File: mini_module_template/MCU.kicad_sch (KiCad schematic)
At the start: 35 parts, among them J3 SWD, SW1 USR_BTN, SW2 BOOT0, SW3 NRST, U1 STM32F303CBTx, U2 FM24CL16B, Y1 8MHz

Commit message: Leyout rev 1
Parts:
- removed J3: SWD, Connector_PinHeader_2.54mm:PinHeader_1x04_P2.54mm_Vertical, symbol Connector_Generic:Conn_01x04
- removed R10, R13, R17: 10k, Resistor_SMD:R_0402_1005Metric, symbol Device:R
- added J1: SWD, Connector_PinSocket_2.54mm:PinSocket_1x05_P2.54mm_Vertical, symbol Connector_Generic:Conn_01x05
- C11: renamed from C3; value 16p -> 17p
- C12: renamed from C4; value 16p -> 17p
- R1: renamed from R15; now not fitted
- R8: renamed from R3; now not fitted
- SW1: renamed from SW2; footprint Button_Switch_SMD:SW_SPST_PTS810 -> Button_Switch_THT:SW_Tactile_SPST_Angled_PTS645Vx58-2LFS; now not fitted
- SW2: renamed from SW3; footprint Button_Switch_SMD:SW_SPST_PTS810 -> Button_Switch_THT:SW_Tactile_SPST_Angled_PTS645Vx58-2LFS
- SW3: renamed from SW1; footprint Button_Switch_SMD:SW_SPST_PTS810 -> Button_Switch_THT:SW_Tactile_SPST_Angled_PTS645Vx58-2LFS; now not fitted
- renumbered C5 to C1, C1 to C10, C6 to C2, C7 to C3, C8 to C4, C9 to C5, C10 to C6, C11 to C7, C12 to C8, C2 to C9, D1 to D2, D2 to D3, R2 to R10, R19 to R2, R12 to R3, R16 to R4, R11 to R5, R14 to R6, R18 to R7, R1 to R9
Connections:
- net +3V3: now also J1.1 (Pin_1)
- net GND: now also J1.5 (Pin_5)
- net NRST: now also J1.2 (Pin_2)
- net SWCLK: now also J1.4 (Pin_4)
- net SWDIO: now also J1.3 (Pin_3)
- net PA15: no longer names the net of U1.38 (PA15)
- no-connect marks 0 -> 4
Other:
- note removed: "optional pulldown resistors"
- moved on the sheet: R7, U2

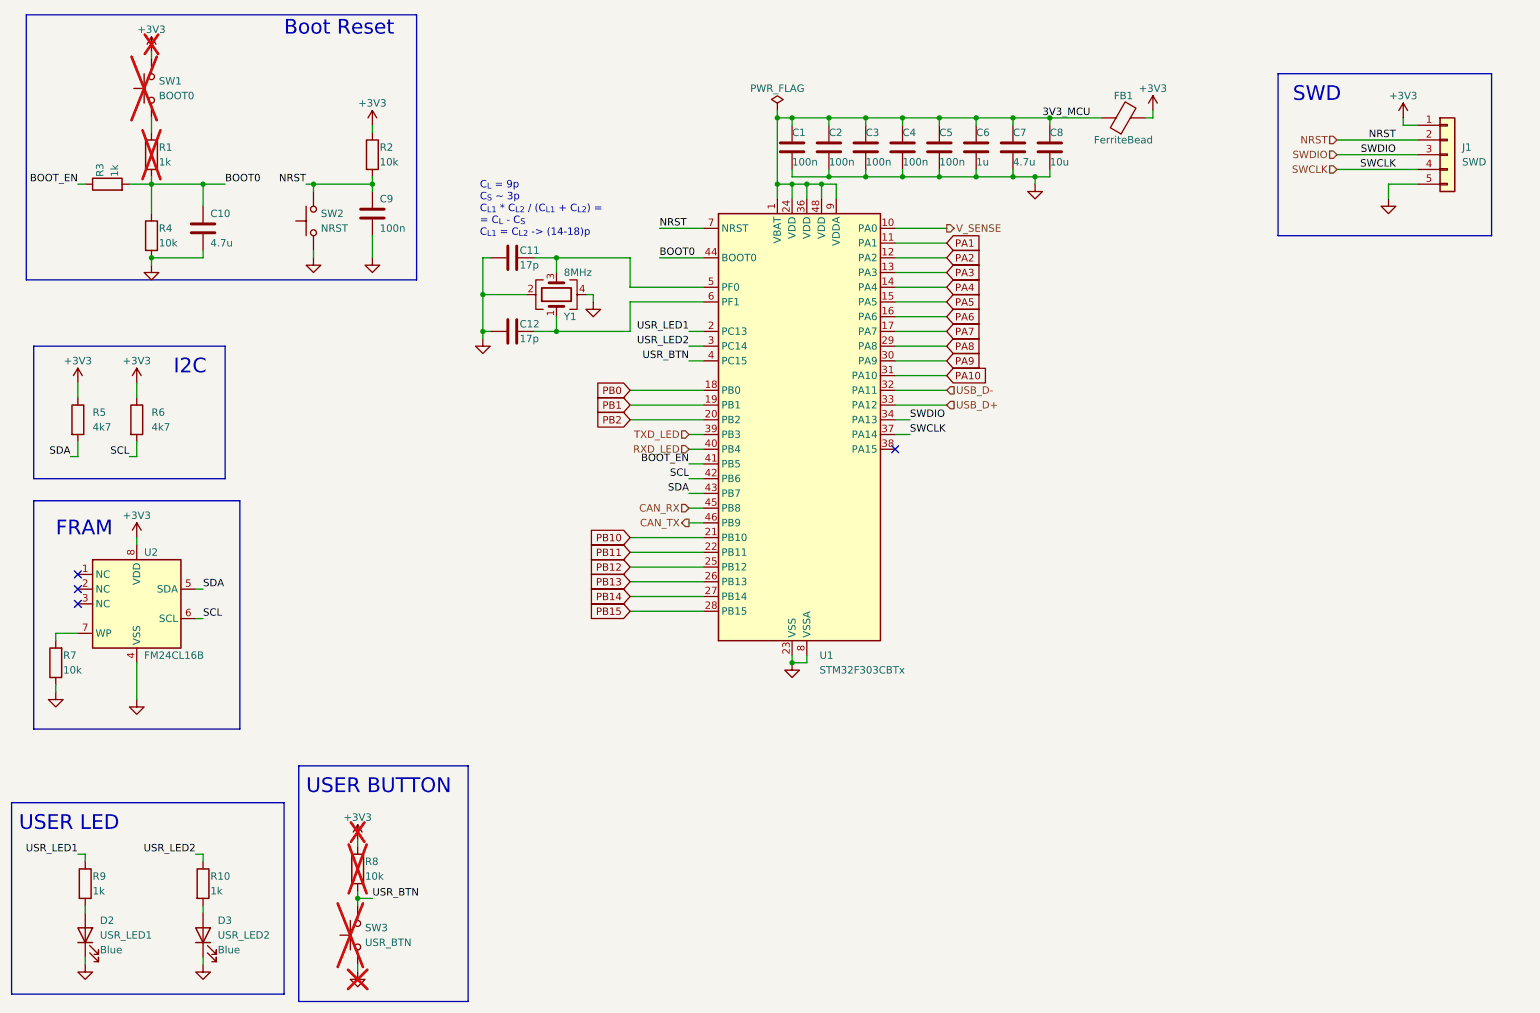
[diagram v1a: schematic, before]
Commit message: revison C, aded 2 can support and gight voltage input stepdown
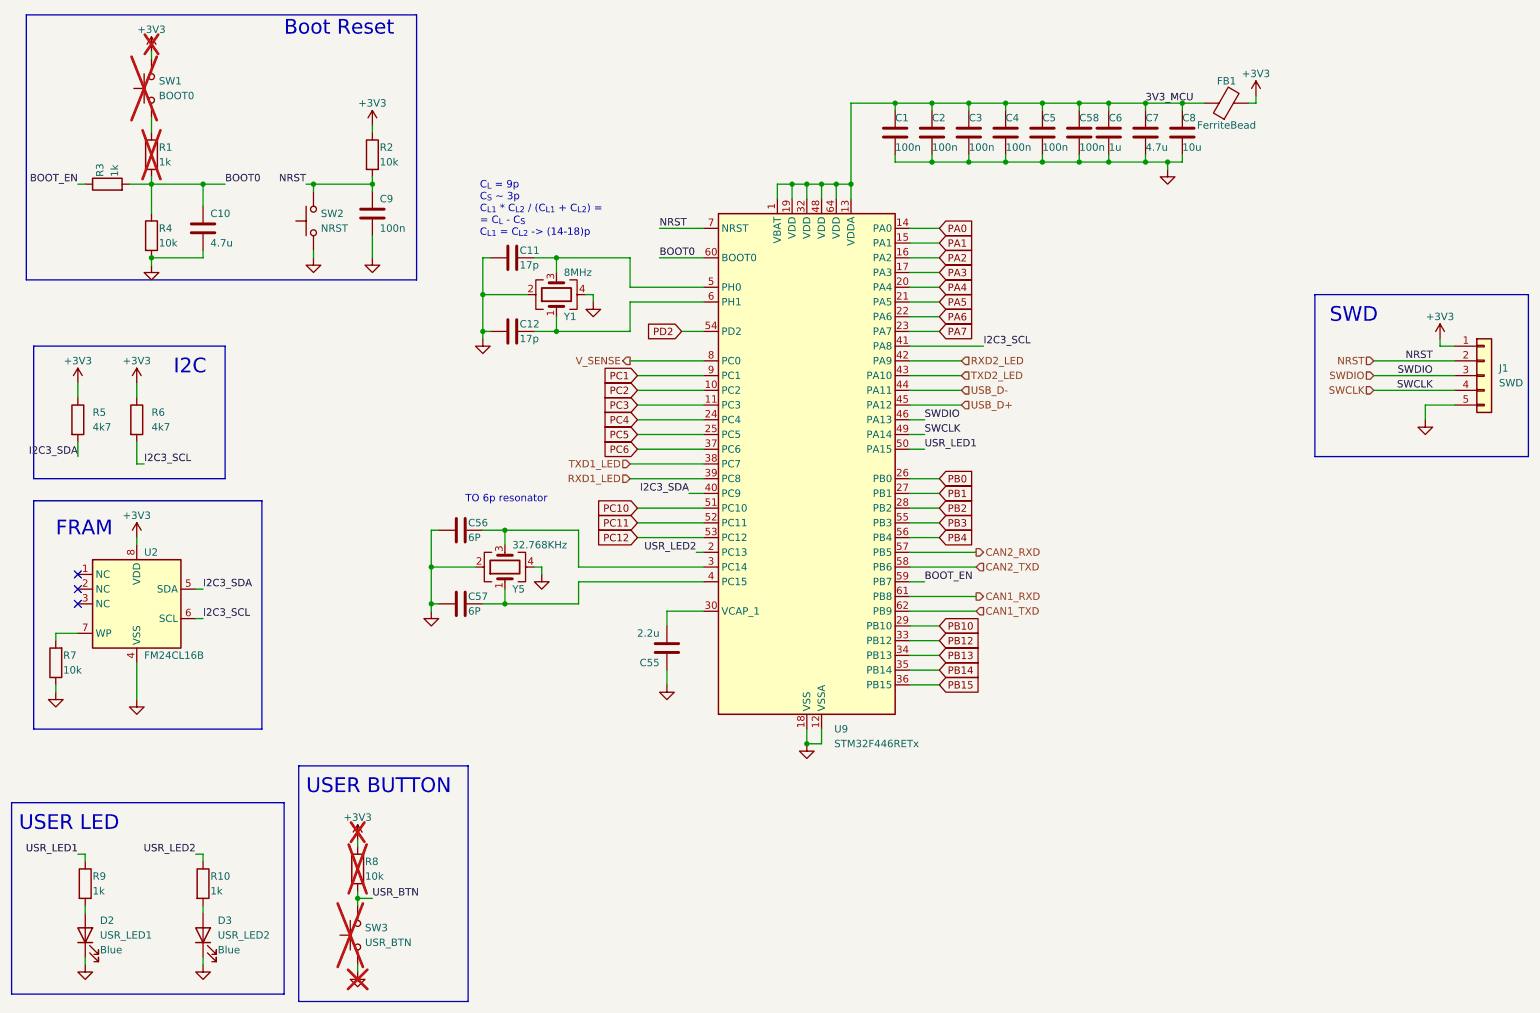
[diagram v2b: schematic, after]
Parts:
- removed U1: STM32F303CBTx, Package_QFP:LQFP-48_7x7mm_P0.5mm, symbol MCU_ST_STM32F3:STM32F303CBTx
- added C55: 2.2u, Capacitor_SMD:C_0603_1608Metric, symbol Device:C
- added C56, C57: 6P, Capacitor_SMD:C_0402_1005Metric, symbol Device:C
- added C58: 100n, Capacitor_SMD:C_0402_1005Metric, symbol Device:C
- added U9: STM32F446RETx, Package_QFP:LQFP-64_10x10mm_P0.5mm, symbol MCU_ST_STM32F4:STM32F446RETx
- added Y5: 32.768KHz, Crystal:Crystal_SMD_3225-4Pin_3.2x2.5mm, symbol Device:Crystal_GND24
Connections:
- net 3V3_MCU: now also C58.1, U9.1 (VBAT), U9.13 (VDDA), U9.19 (VDD), U9.32 (VDD), U9.48 (VDD), U9.64 (VDD)
- net BOOT0: now also U9.60 (BOOT0)
- net BOOT_EN: now also U9.59 (PB7)
- net GND: now also C55.1, C56.1, C57.1, C58.2, U9.12 (VSSA), U9.18 (VSS), U9.31 (VSS), U9.47 (VSS), U9.63 (VSS), Y5.2, Y5.4
- net NRST: now also U9.7 (NRST)
- net PA1: now also U9.15 (PA1)
- net PA2: now also U9.16 (PA2)
- net PA3: now also U9.17 (PA3)
- net PA4: now also U9.20 (PA4)
- net PA5: now also U9.21 (PA5)
- net PA6: now also U9.22 (PA6)
- net PA7: now also U9.23 (PA7)
- net PB0: now also U9.26 (PB0)
- net PB1: now also U9.27 (PB1)
- net PB10: now also U9.29 (PB10)
- net PB12: now also U9.33 (PB12)
- net PB13: now also U9.34 (PB13)
- net PB14: now also U9.35 (PB14)
- net PB15: now also U9.36 (PB15)
- net PB2: now also U9.28 (PB2)
- net SWCLK: now also U9.49 (PA14)
- net SWDIO: now also U9.46 (PA13)
- net USB_D+: now also U9.45 (PA12)
- net USB_D-: now also U9.44 (PA11)
- net USR_LED1: now also U9.50 (PA15)
- net USR_LED2: now also U9.2 (PC13)
- net V_SENSE: now also U9.8 (PC0)
- net at C12.2, Y1.1: now also U9.6 (PH1)
- net at C11.2, Y1.3: now also U9.5 (PH0)
- net SCL renamed I2C3_SCL
- net I2C3_SCL: now also U9.41 (PA8)
- net SDA renamed I2C3_SDA
- net I2C3_SDA: now also U9.40 (PC9)
- new net: C57.2, U9.4 (PC15), Y5.1
- new net: C56.2, U9.3 (PC14), Y5.3
- new net: C55.2, U9.30 (VCAP_1)
- new net CAN1_RXD: U9.61 (PB8)
- new net CAN1_TXD: U9.62 (PB9)
- new net CAN2_RXD: U9.57 (PB5)
- new net CAN2_TXD: U9.58 (PB6)
- new net PA0: U9.14 (PA0)
- new net PB3: U9.55 (PB3)
- new net PB4: U9.56 (PB4)
- new net PC1: U9.9 (PC1)
- new net PC10: U9.51 (PC10)
- new net PC11: U9.52 (PC11)
- new net PC12: U9.53 (PC12)
- new net PC2: U9.10 (PC2)
- new net PC3: U9.11 (PC3)
- new net PC4: U9.24 (PC4)
- new net PC5: U9.25 (PC5)
- new net PC6: U9.37 (PC6)
- new net PD2: U9.54 (PD2)
- new net RXD1_LED: U9.39 (PC8)
- new net RXD2_LED: U9.42 (PA9)
- new net TXD1_LED: U9.38 (PC7)
- new net TXD2_LED: U9.43 (PA10)
- no-connect marks 4 -> 3
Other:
- note added: "TO 6p resonator"
- moved on the sheet: C1, C2, C3, C4, C5, C6, C7, C8, FB1, J1

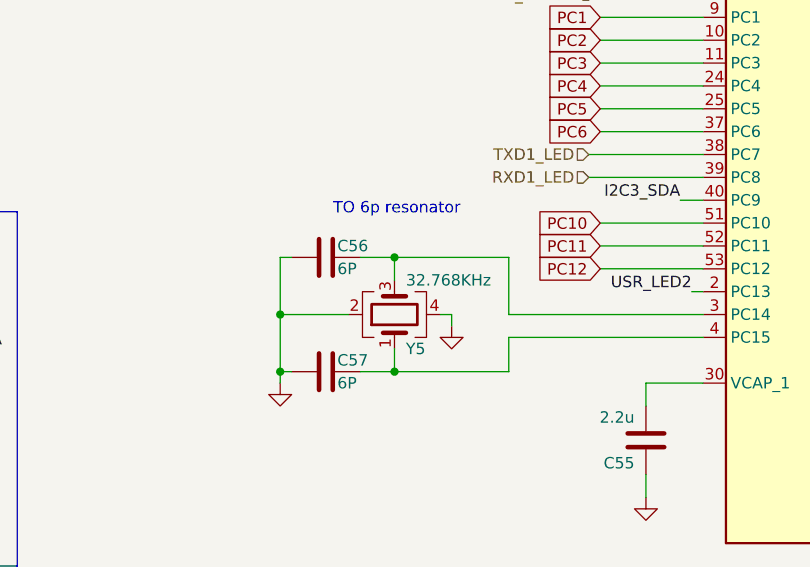
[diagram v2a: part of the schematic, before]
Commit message: changed rj45 conenctor to use differnt pinout with can
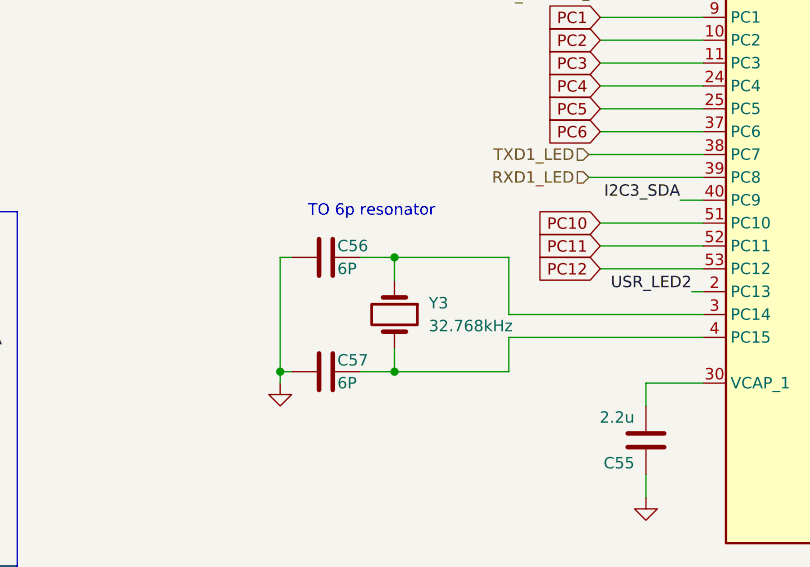
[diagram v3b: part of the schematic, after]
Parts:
- removed Y5: 32.768KHz, Crystal:Crystal_SMD_3225-4Pin_3.2x2.5mm, symbol Device:Crystal_GND24
- added Y3: 32.768kHz, Crystal:Crystal_SMD_3215-2Pin_3.2x1.5mm, symbol Device:Crystal
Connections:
- net at C57.2, U9.4 (PC15): now also Y3.2
- net at C56.2, U9.3 (PC14): now also Y3.1
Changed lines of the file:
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@@
 	)
 	(junction
-		(at 90.17 113.03)
-		(diameter 0)
-		(color 0 0 0 0)
-	)
-	(junction
 		(at 154.94 143.51)
 		(diameter 0)
@@
 	(wire
 		(pts
-			(xy 90.17 113.03) (xy 97.79 113.03)
-		)
-		(stroke
-			(width 0)
-			(type default)
-		)
-	)
-	(wire
-		(pts
 			(xy 125.73 102.87) (xy 137.16 102.87)
 		)
@@
 	(wire
 		(pts
-			(xy 90.17 113.03) (xy 90.17 119.38)
-		)
-		(stroke
-			(width 0)
-			(type default)
-		)
-	)
-	(wire
-		(pts
 			(xy 172.72 87.63) (xy 175.26 87.63)
 		)
@@
 	(wire
 		(pts
-			(xy 109.22 113.03) (xy 109.22 114.3)
-		)
-		(stroke
-			(width 0)
-			(type default)
-		)
-	)
-	(wire
-		(pts
 			(xy 39.37 81.28) (xy 39.37 83.82)
 		)
@@
 	(wire
 		(pts
-			(xy 107.95 113.03) (xy 109.22 113.03)
-		)
-		(stroke
-			(width 0)
-			(type default)
-		)
-	)
-	(wire
-		(pts
 			(xy 232.41 31.75) (xy 232.41 33.02)
 		)
@@
 	(wire
 		(pts
-			(xy 90.17 106.68) (xy 90.17 113.03)
+			(xy 90.17 106.68) (xy 90.17 119.38)
 		)
 		(stroke
@@
 	(text "TO 6p resonator\n"
 		(exclude_from_sim no)
-		(at 103.124 101.346 0)
+		(at 100.33 101.6 0)
 		(effects
 			(font
@@
 	)
 	(symbol
+		(lib_id "Device:Crystal")
+		(at 102.87 113.03 270)
+		(unit 1)
+		(exclude_from_sim no)
+		(in_bom yes)
+		(on_board yes)
+		(dnp no)
+		(fields_autoplaced yes)
+		(property "Reference" "Y3"
+			(at 106.68 111.7599 90)
+			(effects
+				(font
+					(size 1.27 1.27)
+				)
+				(justify left)
+			)
+		)
+		(property "Value" "32.768kHz"
+			(at 106.68 114.2999 90)
+			(effects
+				(font
+					(size 1.27 1.27)
+				)
+				(justify left)
+			)
+		)
+		(property "Footprint" "Crystal:Crystal_SMD_3215-2Pin_3.2x1.5mm"
+			(at 102.87 113.03 0)
+			(effects
+				(font
+					(size 1.27 1.27)
+				)
+				(hide yes)
+			)
+		)
+		(property "Datasheet" "~"
+			(at 102.87 113.03 0)
+			(effects
+				(font
+					(size 1.27 1.27)
+				)
+				(hide yes)
+			)
+		)
+		(property "Description" "Two pin crystal"
+			(at 102.87 113.03 0)
+			(effects
+				(font
+					(size 1.27 1.27)
+				)
+				(hide yes)
+			)
+		)
+		(pin "1"
+		)
+		(pin "2"
+		)
+		(instances
+			(project ""
+				(path "/f131027f-631c-4099-b0ec-5f883860005f/a4b9441c-60f3-49e8-82a9-f2ebbfa51587"
+					(reference "Y3")
+					(unit 1)
+				)
+			)
+		)
+	)
+	(symbol
 		(lib_id "Switch:SW_Push")
 		(at 69.85 53.34 90)
@@
 	)
 	(symbol
-		(lib_id "Device:Crystal_GND24")
-		(at 102.87 113.03 90)
-		(unit 1)
-		(exclude_from_sim no)
-		(in_bom yes)
-		(on_board yes)
-		(dnp no)
-		(property "Reference" "Y5"
-			(at 104.14 116.84 90)
-			(effects
-				(font
-					(size 1.27 1.27)
-				)
-				(justify right)
-			)
-		)
-		(property "Value" "32.768KHz"
-			(at 104.14 109.22 90)
-			(effects
-				(font
-					(size 1.27 1.27)
-				)
-				(justify right)
-			)
-		)
-		(property "Footprint" "Crystal:Crystal_SMD_3225-4Pin_3.2x2.5mm"
-			(at 102.87 113.03 0)
-			(effects
-				(font
-					(size 1.27 1.27)
-				)
-				(hide yes)
-			)
-		)
-		(property "Datasheet" "~"
-			(at 102.87 113.03 0)
-			(effects
-				(font
-					(size 1.27 1.27)
-				)
-				(hide yes)
-			)
-		)
-		(property "Description" ""
-			(at 102.87 113.03 0)
-			(effects
-				(font
-					(size 1.27 1.27)
-				)
-				(hide yes)
-			)
-		)
-		(pin "1"
-		)
-		(pin "2"
-		)
-		(pin "3"
-		)
-		(pin "4"
-		)
-		(instances
-			(project "mini_module_template"
-				(path "/f131027f-631c-4099-b0ec-5f883860005f/a4b9441c-60f3-49e8-82a9-f2ebbfa51587"
-					(reference "Y5")
-					(unit 1)
-				)
-			)
-		)
-	)
-	(symbol
 		(lib_id "Device:R")
 		(at 34.29 46.99 90)
@@
 					(unit 1)
 				)
-			)
-		)
-	)
-	(symbol
-		(lib_id "power:GND")
-		(at 109.22 114.3 0)
-		(unit 1)
-		(exclude_from_sim no)
-		(in_bom yes)
-		(on_board yes)
-		(dnp no)
-		(property "Reference" "#PWR0105"
-			(at 109.22 120.65 0)
-			(effects
-				(font
-					(size 1.27 1.27)
-				)
-				(hide yes)
-			)
-		)
-		(property "Value" "GND"
-			(at 109.22 118.11 0)
-			(effects
-				(font
-					(size 1.27 1.27)
-				)
-				(hide yes)
-			)
-		)
-		(property "Footprint" ""
-			(at 109.22 114.3 0)
-			(effects
-				(font
-					(size 1.27 1.27)
-				)
-				(hide yes)
-			)
-		)
-		(property "Datasheet" ""
-			(at 109.22 114.3 0)
-			(effects
-				(font
-					(size 1.27 1.27)
-				)
-				(hide yes)
-			)
-		)
-		(property "Description" ""
-			(at 109.22 114.3 0)
-			(effects
-				(font
-					(size 1.27 1.27)
-				)
-				(hide yes)
-			)
-		)
-		(pin "1"
-		)
-		(instances
-			(project "mini_module_template"
-				(path "/f131027f-631c-4099-b0ec-5f883860005f/a4b9441c-60f3-49e8-82a9-f2ebbfa51587"
-					(reference "#PWR0105")
-					(unit 1)
-				)

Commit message: final check rev A
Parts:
- C55: footprint Capacitor_SMD:C_0603_1608Metric -> Capacitor_SMD:C_0402_1005Metric
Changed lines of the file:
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@@
 			)
 		)
-		(property "Footprint" "Capacitor_SMD:C_0603_1608Metric"
+		(property "Footprint" "Capacitor_SMD:C_0402_1005Metric"
 			(at 129.8448 123.19 0)
 			(effects

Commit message: updaet schematic
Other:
- company: (none) -> Patryk Dudziński
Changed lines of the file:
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@@
 	(title_block
 		(title "MCU")
+		(date "2025-01-10")
+		(rev "1.0")
+		(company "Patryk Dudziński")
 	)
 	(junction
@@
 	(label "I2C3_SDA"
 		(at 29.21 93.98 180)
-		(fields_autoplaced yes)
 		(effects
 			(font
@@
 	(label "NRST"
 		(at 129.54 54.61 0)
-		(fields_autoplaced yes)
 		(effects
 			(font
@@
 	(label "BOOT_EN"
 		(at 175.26 115.57 0)
-		(fields_autoplaced yes)
 		(effects
 			(font
@@
 	(label "SWDIO"
 		(at 262.89 80.01 180)
-		(fields_autoplaced yes)
 		(effects
 			(font
@@
 	(label "BOOT0"
 		(at 129.54 59.69 0)
-		(fields_autoplaced yes)
 		(effects
 			(font
@@
 	(label "I2C3_SDA"
 		(at 50.8 116.84 0)
-		(fields_autoplaced yes)
 		(effects
 			(font
@@
 	(label "I2C3_SCL"
 		(at 50.8 121.92 0)
-		(fields_autoplaced yes)
 		(effects
 			(font
@@
 	(label "USR_LED2"
 		(at 135.89 110.49 180)
-		(fields_autoplaced yes)
 		(effects
 			(font
@@
 	(label "BOOT_EN"
 		(at 29.21 46.99 180)
-		(fields_autoplaced yes)
 		(effects
 			(font
@@
 	(label "USR_BTN"
 		(at 80.01 170.18 0)
-		(fields_autoplaced yes)
 		(effects
 			(font
@@
 	(label "3V3_MCU"
 		(at 213.36 33.02 0)
-		(fields_autoplaced yes)
 		(effects
 			(font
@@
 	(label "I2C3_SCL"
 		(at 40.64 95.25 0)
-		(fields_autoplaced yes)
 		(effects
 			(font
@@
 	(label "BOOT0"
 		(at 54.61 46.99 0)
-		(fields_autoplaced yes)
 		(effects
 			(font
@@
 	(label "USR_LED1"
 		(at 29.21 162.56 180)
-		(fields_autoplaced yes)
 		(effects
 			(font
@@
 	(label "USR_LED1"
 		(at 175.26 92.71 0)
-		(fields_autoplaced yes)
 		(effects
 			(font
@@
 	(label "USR_LED2"
 		(at 49.53 162.56 180)
-		(fields_autoplaced yes)
 		(effects
 			(font
@@
 	(label "I2C3_SDA"
 		(at 134.62 100.33 180)
-		(fields_autoplaced yes)
 		(effects
 			(font
@@
 	(label "SWDIO"
 		(at 175.26 87.63 0)
-		(fields_autoplaced yes)
 		(effects
 			(font
@@
 	(label "SWCLK"
 		(at 262.89 82.55 180)
-		(fields_autoplaced yes)
 		(effects
 			(font
@@
 	(label "I2C3_SCL"
 		(at 185.42 74.93 0)
-		(fields_autoplaced yes)
 		(effects
 			(font
@@
 	(label "NRST"
 		(at 262.89 77.47 180)
-		(fields_autoplaced yes)
 		(effects
 			(font
@@
 	(label "NRST"
 		(at 68.58 46.99 180)
-		(fields_autoplaced yes)
 		(effects
 			(font
@@
 	(label "SWCLK"
 		(at 175.26 90.17 0)
-		(fields_autoplaced yes)
 		(effects
 			(font
@@
 		(shape input)
 		(at 181.61 80.01 0)
-		(fields_autoplaced yes)
 		(effects
 			(font
@@
 		(shape input)
 		(at 124.46 95.25 180)
-		(fields_autoplaced yes)
 		(effects
 			(font
@@
 		(shape input)
 		(at 252.73 77.47 180)
-		(fields_autoplaced yes)
 		(effects
 			(font
@@
 		(shape output)
 		(at 184.15 110.49 0)
-		(fields_autoplaced yes)
 		(effects
 			(font
@@
 		(shape output)
 		(at 184.15 118.11 0)
-		(fields_autoplaced yes)
 		(effects
 			(font
@@
 		(shape input)
 		(at 181.61 77.47 0)
-		(fields_autoplaced yes)
 		(effects
 			(font
@@
 		(shape input)
 		(at 181.61 85.09 0)
-		(fields_autoplaced yes)
 		(effects
 			(font
@@
 		(shape input)
 		(at 124.46 97.79 180)
-		(fields_autoplaced yes)
 		(effects
 			(font
@@
 		(shape input)
 		(at 181.61 82.55 0)
-		(fields_autoplaced yes)
 		(effects
 			(font
@@
 		(shape input)
 		(at 184.15 120.65 0)
-		(fields_autoplaced yes)
 		(effects
 			(font
@@
 		(shape input)
 		(at 252.73 82.55 180)
-		(fields_autoplaced yes)
 		(effects
 			(font
@@
 		(shape input)
 		(at 252.73 80.01 180)
-		(fields_autoplaced yes)
 		(effects
 			(font
@@
 		(shape output)
 		(at 124.46 77.47 180)
-		(fields_autoplaced yes)
 		(effects
 			(font
@@
 		(shape input)
 		(at 184.15 113.03 0)
-		(fields_autoplaced yes)
 		(effects
 			(font
